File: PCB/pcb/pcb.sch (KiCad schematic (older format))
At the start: 13 parts, among them SW1 SW_Push, U1 ATmega32U4-AU, X1 Crystal_GND2

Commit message: Refactor controller layout.
Think that this is pretty much complete now.

Next up the matrix
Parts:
- removed R1: 10k, symbol Device:R
- removed X1: Crystal_GND2, symbol Device:Crystal_GND2
- added C7: 1u, symbol Device:C_Small
- added J1: USB_B_Micro, symbol Connector:USB_B_Micro
- added R1: 330, symbol Device:R_Small
- added R2: R_Small, symbol Device:R_Small
- added R3, R4: 10k, symbol Device:R_Small
- added Y1: 16MHz, symbol Device:Crystal_Small
- C1: renamed from C8; value 0.1u -> 11n
- R5: renamed from R2; value 10k -> 1k
- renumbered C3 to C2, C4 to C3, C1 to C4, C2 to C5, C5 to C6, C6 to C8, C7 to C9
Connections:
- net labels added: +5V, RST
- net labels removed: RESET, VCC, XTAL1, XTAL2
- wire segments 31 -> 47
- no-connect marks 0 -> 2
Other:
- note removed: "Crystal - Clock"
- note removed: "Reset button"
- note removed: "VCC - Decoupling caps"
- moved on the sheet: C1, C2, C3, C4, C5, C6, C8, C9, R5, SW1, U1

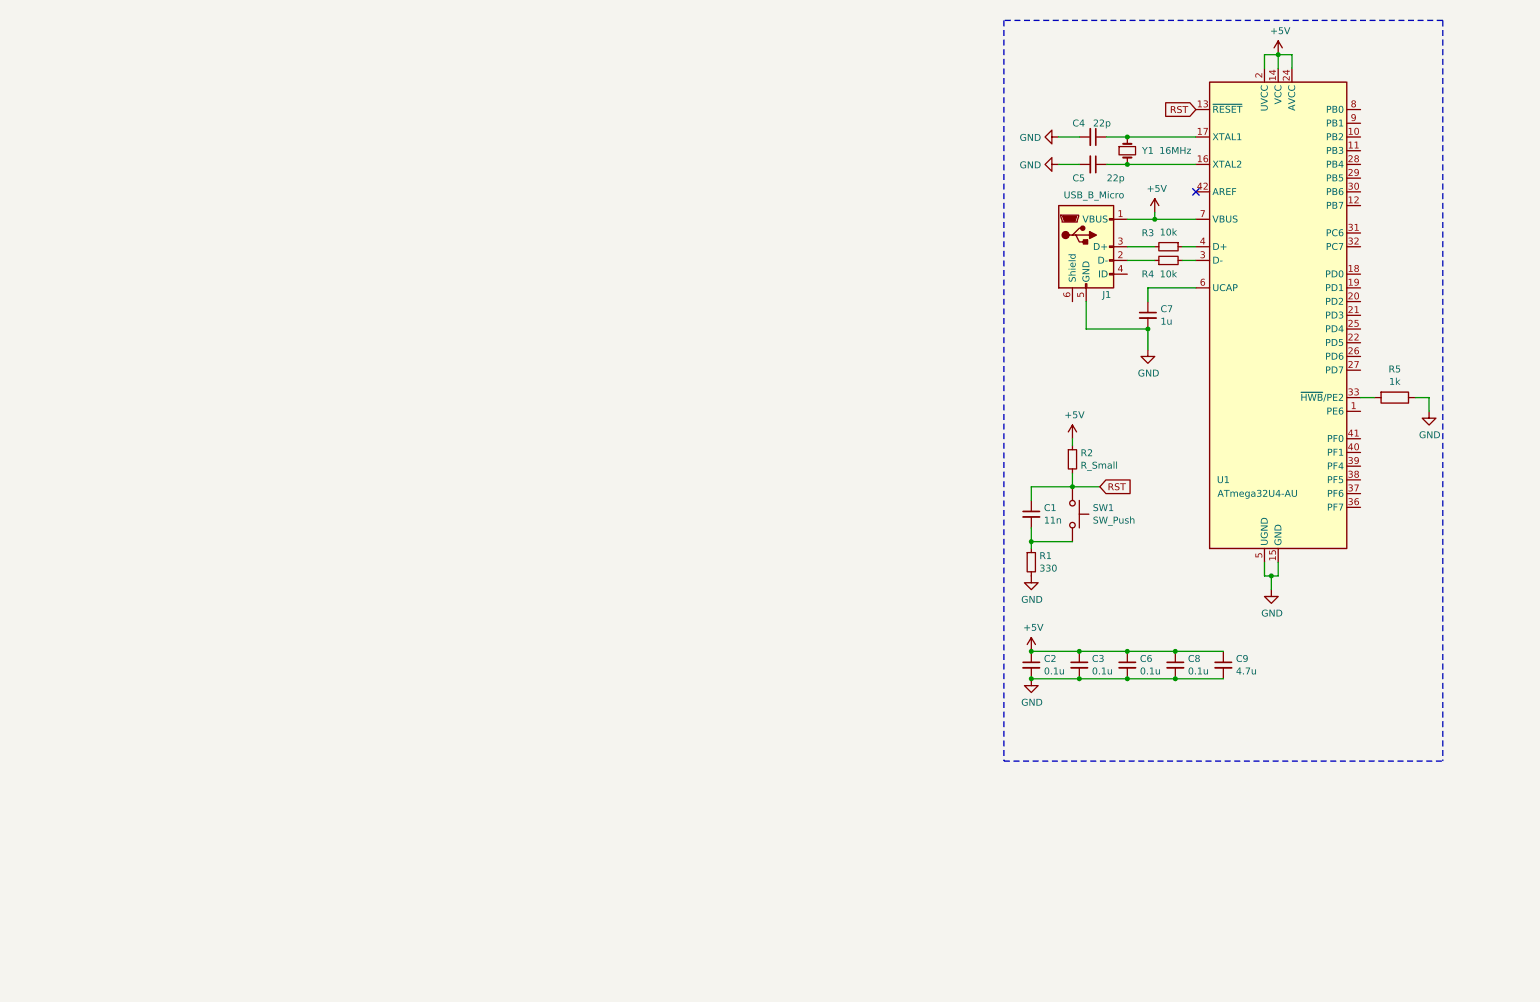
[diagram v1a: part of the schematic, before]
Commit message: Build the switch Matrix based on kbfirmwarebuilder
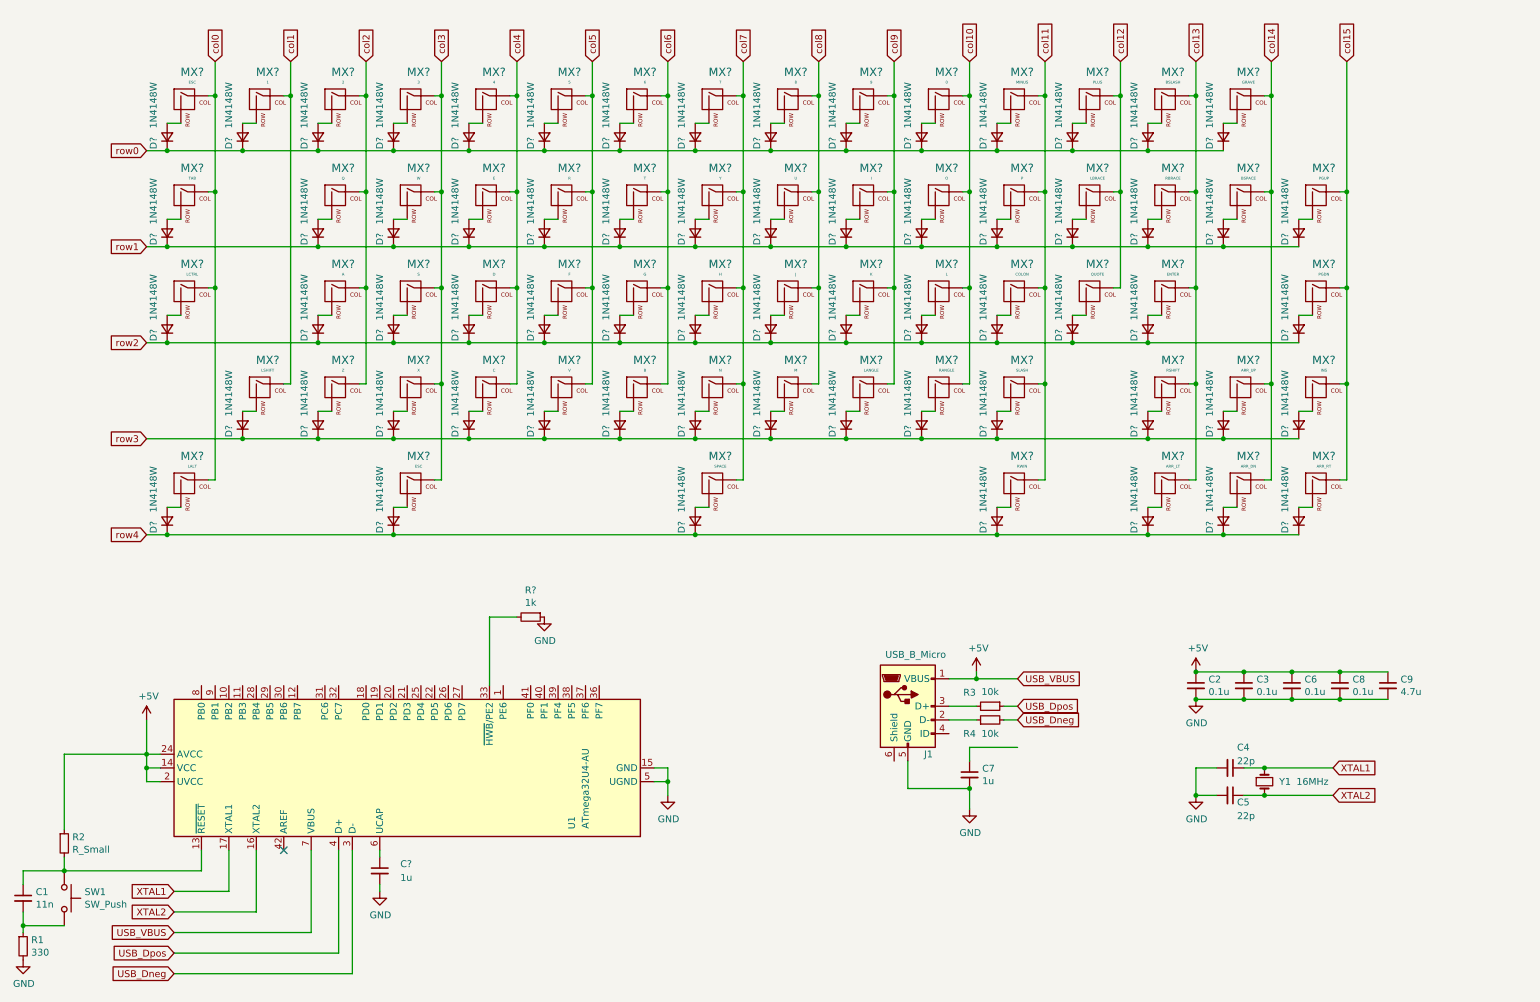
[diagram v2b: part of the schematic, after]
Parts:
- removed R5: 1k, symbol Device:R
- added C?: 1u, symbol Device:C_Small
- added D? (x65): 1N4148W, symbol Device:D_Small
- added MX? (x2): ESC, symbol MX_Alps_Hybrid:MX-NoLED
- added MX?: 1, symbol MX_Alps_Hybrid:MX-NoLED
- added MX?: 2, symbol MX_Alps_Hybrid:MX-NoLED
- added MX?: 3, symbol MX_Alps_Hybrid:MX-NoLED
- added MX?: 4, symbol MX_Alps_Hybrid:MX-NoLED
- added MX?: 5, symbol MX_Alps_Hybrid:MX-NoLED
- added MX?: 6, symbol MX_Alps_Hybrid:MX-NoLED
- added MX?: 7, symbol MX_Alps_Hybrid:MX-NoLED
- added MX?: 8, symbol MX_Alps_Hybrid:MX-NoLED
- added MX?: 9, symbol MX_Alps_Hybrid:MX-NoLED
- added MX?: 0, symbol MX_Alps_Hybrid:MX-NoLED
- added MX?: MINUS, symbol MX_Alps_Hybrid:MX-NoLED
- added MX?: PLUS, symbol MX_Alps_Hybrid:MX-NoLED
- added MX?: BSLASH, symbol MX_Alps_Hybrid:MX-NoLED
- added MX?: TAB, symbol MX_Alps_Hybrid:MX-NoLED
- added MX?: GRAVE, symbol MX_Alps_Hybrid:MX-NoLED
- added MX?: Q, symbol MX_Alps_Hybrid:MX-NoLED
- added MX?: W, symbol MX_Alps_Hybrid:MX-NoLED
- added MX?: E, symbol MX_Alps_Hybrid:MX-NoLED
- added MX?: R, symbol MX_Alps_Hybrid:MX-NoLED
- added MX?: T, symbol MX_Alps_Hybrid:MX-NoLED
- added MX?: Y, symbol MX_Alps_Hybrid:MX-NoLED
- added MX?: U, symbol MX_Alps_Hybrid:MX-NoLED
- added MX?: I, symbol MX_Alps_Hybrid:MX-NoLED
- added MX?: O, symbol MX_Alps_Hybrid:MX-NoLED
- added MX?: P, symbol MX_Alps_Hybrid:MX-NoLED
- added MX?: LBRACE, symbol MX_Alps_Hybrid:MX-NoLED
- added MX?: RBRACE, symbol MX_Alps_Hybrid:MX-NoLED
- added MX?: BSPACE, symbol MX_Alps_Hybrid:MX-NoLED
- added MX?: LCTRL, symbol MX_Alps_Hybrid:MX-NoLED
- added MX?: PGDN, symbol MX_Alps_Hybrid:MX-NoLED
- added MX?: A, symbol MX_Alps_Hybrid:MX-NoLED
- added MX?: S, symbol MX_Alps_Hybrid:MX-NoLED
- added MX?: D, symbol MX_Alps_Hybrid:MX-NoLED
- added MX?: F, symbol MX_Alps_Hybrid:MX-NoLED
- added MX?: G, symbol MX_Alps_Hybrid:MX-NoLED
- added MX?: H, symbol MX_Alps_Hybrid:MX-NoLED
- added MX?: J, symbol MX_Alps_Hybrid:MX-NoLED
- added MX?: K, symbol MX_Alps_Hybrid:MX-NoLED
- added MX?: L, symbol MX_Alps_Hybrid:MX-NoLED
- added MX?: COLON, symbol MX_Alps_Hybrid:MX-NoLED
- added MX?: QUOTE, symbol MX_Alps_Hybrid:MX-NoLED
- added MX?: ENTER, symbol MX_Alps_Hybrid:MX-NoLED
- added MX?: LSHIFT, symbol MX_Alps_Hybrid:MX-NoLED
- added MX?: INS, symbol MX_Alps_Hybrid:MX-NoLED
- added MX?: Z, symbol MX_Alps_Hybrid:MX-NoLED
- added MX?: X, symbol MX_Alps_Hybrid:MX-NoLED
- added MX?: C, symbol MX_Alps_Hybrid:MX-NoLED
- added MX?: V, symbol MX_Alps_Hybrid:MX-NoLED
- added MX?: B, symbol MX_Alps_Hybrid:MX-NoLED
- added MX?: N, symbol MX_Alps_Hybrid:MX-NoLED
- added MX?: M, symbol MX_Alps_Hybrid:MX-NoLED
- added MX?: LANGLE, symbol MX_Alps_Hybrid:MX-NoLED
- added MX?: RANGLE, symbol MX_Alps_Hybrid:MX-NoLED
- added MX?: SLASH, symbol MX_Alps_Hybrid:MX-NoLED
- added MX?: RSHIFT, symbol MX_Alps_Hybrid:MX-NoLED
- added MX?: ARR_UP, symbol MX_Alps_Hybrid:MX-NoLED
- added MX?: LALT, symbol MX_Alps_Hybrid:MX-NoLED
- added MX?: SPACE, symbol MX_Alps_Hybrid:MX-NoLED
- added MX?: RWIN, symbol MX_Alps_Hybrid:MX-NoLED
- added MX?: ARR_LT, symbol MX_Alps_Hybrid:MX-NoLED
- added MX?: ARR_DN, symbol MX_Alps_Hybrid:MX-NoLED
- added MX?: PGUP, symbol MX_Alps_Hybrid:MX-NoLED
- added MX?: ARR_RT, symbol MX_Alps_Hybrid:MX-NoLED
- added R?: 1k, symbol Device:R_Small
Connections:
- net GND: now also C?.2, R?.1
- net XTAL2: now reaches C5.1, U1.16 (XTAL2), Y1.2
- net XTAL1: now reaches C4.1, U1.17 (XTAL1), Y1.1
- net USB_Dneg: now reaches R4.2, U1.3 (D-)
- net at U1.33 (~HWB~/PE2): now also R?.2
- net USB_Dpos: now reaches R3.1, U1.4 (D+)
- net at U1.6 (UCAP): now also C?.1; no longer C7.1
- net RST: no longer names the net of C1.1, R2.2, SW1.1, U1.13 (~RESET)
- new net: D?.2 (A), MX?.2 (ROW) (x65)
- new net col0: MX?.1 (COL), MX?.1 (COL), MX?.1 (COL), MX?.1 (COL)
- new net col1: MX?.1 (COL), MX?.1 (COL)
- new net col10: MX?.1 (COL), MX?.1 (COL), MX?.1 (COL), MX?.1 (COL)
- new net col11: MX?.1 (COL), MX?.1 (COL), MX?.1 (COL), MX?.1 (COL), MX?.1 (COL)
- new net col12: MX?.1 (COL), MX?.1 (COL), MX?.1 (COL)
- new net col13: MX?.1 (COL), MX?.1 (COL), MX?.1 (COL), MX?.1 (COL), MX?.1 (COL)
- new net col14: MX?.1 (COL), MX?.1 (COL), MX?.1 (COL), MX?.1 (COL)
- new net col15: MX?.1 (COL), MX?.1 (COL), MX?.1 (COL), MX?.1 (COL)
- new net col2: MX?.1 (COL), MX?.1 (COL), MX?.1 (COL), MX?.1 (COL)
- new net col3: MX?.1 (COL), MX?.1 (COL), MX?.1 (COL), MX?.1 (COL), MX?.1 (COL)
- new net col4: MX?.1 (COL), MX?.1 (COL), MX?.1 (COL), MX?.1 (COL)
- new net col5: MX?.1 (COL), MX?.1 (COL), MX?.1 (COL), MX?.1 (COL)
- new net col6: MX?.1 (COL), MX?.1 (COL), MX?.1 (COL), MX?.1 (COL)
- new net col7: MX?.1 (COL), MX?.1 (COL), MX?.1 (COL), MX?.1 (COL), MX?.1 (COL)
- new net col8: MX?.1 (COL), MX?.1 (COL), MX?.1 (COL), MX?.1 (COL)
- new net col9: MX?.1 (COL), MX?.1 (COL), MX?.1 (COL), MX?.1 (COL)
- new net row0: D?.1 (K), D?.1 (K), D?.1 (K), D?.1 (K), D?.1 (K), D?.1 (K), D?.1 (K), D?.1 (K), D?.1 (K), D?.1 (K), D?.1 (K), D?.1 (K), D?.1 (K), D?.1 (K), D?.1 (K)
- new net row1: D?.1 (K), D?.1 (K), D?.1 (K), D?.1 (K), D?.1 (K), D?.1 (K), D?.1 (K), D?.1 (K), D?.1 (K), D?.1 (K), D?.1 (K), D?.1 (K), D?.1 (K), D?.1 (K), D?.1 (K)
- new net row2: D?.1 (K), D?.1 (K), D?.1 (K), D?.1 (K), D?.1 (K), D?.1 (K), D?.1 (K), D?.1 (K), D?.1 (K), D?.1 (K), D?.1 (K), D?.1 (K), D?.1 (K), D?.1 (K)
- new net row3: D?.1 (K), D?.1 (K), D?.1 (K), D?.1 (K), D?.1 (K), D?.1 (K), D?.1 (K), D?.1 (K), D?.1 (K), D?.1 (K), D?.1 (K), D?.1 (K), D?.1 (K), D?.1 (K)
- new net row4: D?.1 (K), D?.1 (K), D?.1 (K), D?.1 (K), D?.1 (K), D?.1 (K), D?.1 (K)
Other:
- moved on the sheet: C1, C2, C3, C4, C5, C6, C7, C8, C9, J1, R1, R2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

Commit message: reset annotations
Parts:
- removed C7: 1u, symbol Device:C_Small
- C1: value 11n -> 100n
- MX15: renamed from MX?; value ESC -> LWIN_1.5
- MX2: renamed from MX?; value TAB -> TAB_1.5
- MX3: renamed from MX?; value LCTRL -> LCTRL_1.75
- MX32: renamed from MX?; value SPACE -> SPACE_7flipped
- MX4: renamed from MX?; value LALT -> LALT_1.5
- MX49: renamed from MX?; value RWIN -> RWIN_1.5
- MX55: renamed from MX?; value ENTER -> ENTER_2.25
- MX56: renamed from MX?; value RSHIFT -> RSHIFT_1.75
- MX59: renamed from MX?; value BSPACE -> BSPACE_1.5
- MX6: renamed from MX?; value LSHIFT -> LSHIFT_2.25
- gave numbers to parts that had none: 122
- renumbered C9 to C10, C2 to C4, C4 to C5, C5 to C6, C3 to C7, C6 to C8, C8 to C9, R3 to R4, R4 to R5
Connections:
- net GND: now also C1.2, J1.6 (Shield)
- net col0: now also U1.29 (PB5)
- net col1: now also U1.30 (PB6)
- net col10: now also U1.22 (PD5)
- net col11: now also U1.26 (PD6)
- net col12: now also U1.27 (PD7)
- net col13: now also U1.41 (PF0)
- net col14: now also U1.40 (PF1)
- net col15: now also U1.39 (PF4)
- net col2: now also U1.12 (PB7)
- net col3: now also U1.31 (PC6)
- net col4: now also U1.32 (PC7)
- net col5: now also U1.18 (PD0)
- net col6: now also U1.19 (PD1)
- net col7: now also U1.20 (PD2)
- net col8: now also U1.21 (PD3)
- net col9: now also U1.25 (PD4)
- net row0: now also U1.8 (PB0)
- net row1: now also U1.9 (PB1)
- net row2: now also U1.10 (PB2)
- net row3: now also U1.11 (PB3)
- net row4: now also U1.28 (PB4)
- net at R1.1, SW1.2: no longer C1.2
- no-connect marks 2 -> 7
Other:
- moved on the sheet: R1

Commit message: Add footprints
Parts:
- C1, C10, C2, C4, C5, C6, C7, C8, C9: footprint (none) -> Capacitor_SMD:C_0805_2012Metric_Pad1.15x1.40mm_HandSolder
- D1, D10, D11, D12, D13, D14, D15, D16, D17, D18, D19, D2, D20, D21, D22, D23, D24, D25, D26, D27, D28, D29, D3, D30, D31, D32, D33, D34, D35, D36, D37, D38, D39, D4, D40, D41, D42, D43, D44, D45, D46, D47, D48, D49, D5, D50, D51, D52, D53, D54, D55, D56, D57, D58, D59, D6, D60, D61, D62, D63, D64, D65, D7, D8, D9: footprint (none) -> Diode_SMD:D_SOD-123
- J1: footprint (none) -> Connector_USB:USB_Micro-B_GCT_USB3076-30-A
- MX1, MX10, MX11, MX12, MX13, MX14, MX16, MX17, MX18, MX19, MX20, MX21, MX22, MX23, MX24, MX25, MX26, MX27, MX28, MX29, MX30, MX31, MX33, MX34, MX35, MX36, MX37, MX38, MX39, MX40, MX41, MX42, MX43, MX44, MX45, MX46, MX47, MX48, MX49, MX5, MX50, MX51, MX52, MX53, MX54, MX57, MX58, MX60, MX61, MX62, MX63, MX64, MX65, MX7, MX8, MX9: footprint (none) -> MX_Only:MXOnly-1U-NoLED
- MX15, MX2, MX4, MX59: footprint (none) -> MX_Only:MXOnly-1.5U-NoLED
- MX3, MX56: footprint (none) -> MX_Only:MXOnly-1.75U-NoLED
- MX32: footprint (none) -> MX_Only:MXOnly-7U-ReversedStabilizers
- MX55, MX6: footprint (none) -> MX_Only:MXOnly-2.25U-NoLED
- R1, R2, R3, R4, R5: footprint (none) -> Resistor_SMD:R_1206_3216Metric_Pad1.42x1.75mm_HandSolder
- SW1: footprint (none) -> Button_Switch_SMD:SW_SPST_B3S-1000
- Y1: footprint (none) -> Crystal:Crystal_SMD_5032-2Pin_5.0x3.2mm_HandSoldering

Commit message: PCB
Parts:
- MX49: footprint MX_Only:MXOnly-1U-NoLED -> MX_Only:MXOnly-1.5U-NoLED
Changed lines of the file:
@@
 F 0 "MX49" H 8033 4173 60  0000 C CNN
 F 1 "RWIN_1.5" H 8033 4099 20  0000 C CNN
-F 2 "MX_Only:MXOnly-1U-NoLED" H 7375 3925 60  0001 C CNN
+F 2 "MX_Only:MXOnly-1.5U-NoLED" H 7375 3925 60  0001 C CNN
 F 3 "" H 7375 3925 60  0001 C CNN
 	1    8000 3950

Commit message: Layout the switches and diodes
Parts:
- removed SW1: SW_Push, Button_Switch_SMD:SW_SPST_B3S-1000, symbol Switch:SW_Push
- removed Y1: 16MHz, Crystal:Crystal_SMD_5032-2Pin_5.0x3.2mm_HandSoldering, symbol Device:Crystal_Small
- added JP1: Jumper_NO_Small, Jumper:SolderJumper-2_P1.3mm_Open_RoundedPad1.0x1.5mm, symbol Device:Jumper_NO_Small
- added Y1: 16MHz, Crystal:Crystal_SMD_5032-4Pin_5.0x3.2mm, symbol Device:Crystal_GND24
- C1: renamed from C4; value 0.1u -> 1u
- C2: renamed from C7; value 0.1u -> 100n
- C3: renamed from C8; value 0.1u -> 100n
- C4: renamed from C9; value 0.1u -> 100n
- C5: renamed from C10; value 4.7u -> 100n
- MX1, MX39, MX56, MX65: symbol MX_Alps_Hybrid:MX-NoLED -> pcb-rescue:MX-NoLED-MX_Alps_Hybrid
- MX10: renamed from MX37; symbol MX_Alps_Hybrid:MX-NoLED -> pcb-rescue:MX-NoLED-MX_Alps_Hybrid
- MX11: renamed from MX41; symbol MX_Alps_Hybrid:MX-NoLED -> pcb-rescue:MX-NoLED-MX_Alps_Hybrid
- MX12: renamed from MX45; symbol MX_Alps_Hybrid:MX-NoLED -> pcb-rescue:MX-NoLED-MX_Alps_Hybrid
- MX13: renamed from MX50; symbol MX_Alps_Hybrid:MX-NoLED -> pcb-rescue:MX-NoLED-MX_Alps_Hybrid
- MX14: renamed from MX53; symbol MX_Alps_Hybrid:MX-NoLED -> pcb-rescue:MX-NoLED-MX_Alps_Hybrid
- MX15: renamed from MX58; symbol MX_Alps_Hybrid:MX-NoLED -> pcb-rescue:MX-NoLED-MX_Alps_Hybrid
- MX16: renamed from MX2; symbol MX_Alps_Hybrid:MX-NoLED -> pcb-rescue:MX-NoLED-MX_Alps_Hybrid
- MX17: renamed from MX8; symbol MX_Alps_Hybrid:MX-NoLED -> pcb-rescue:MX-NoLED-MX_Alps_Hybrid
- MX18: renamed from MX12; symbol MX_Alps_Hybrid:MX-NoLED -> pcb-rescue:MX-NoLED-MX_Alps_Hybrid
- MX19: renamed from MX17; symbol MX_Alps_Hybrid:MX-NoLED -> pcb-rescue:MX-NoLED-MX_Alps_Hybrid
- MX2: renamed from MX5; symbol MX_Alps_Hybrid:MX-NoLED -> pcb-rescue:MX-NoLED-MX_Alps_Hybrid
- MX20: renamed from MX21; symbol MX_Alps_Hybrid:MX-NoLED -> pcb-rescue:MX-NoLED-MX_Alps_Hybrid
- MX21: renamed from MX25; symbol MX_Alps_Hybrid:MX-NoLED -> pcb-rescue:MX-NoLED-MX_Alps_Hybrid
- MX22: renamed from MX29; symbol MX_Alps_Hybrid:MX-NoLED -> pcb-rescue:MX-NoLED-MX_Alps_Hybrid
- MX23: renamed from MX34; symbol MX_Alps_Hybrid:MX-NoLED -> pcb-rescue:MX-NoLED-MX_Alps_Hybrid
- MX24: renamed from MX38; symbol MX_Alps_Hybrid:MX-NoLED -> pcb-rescue:MX-NoLED-MX_Alps_Hybrid
- MX25: renamed from MX42; symbol MX_Alps_Hybrid:MX-NoLED -> pcb-rescue:MX-NoLED-MX_Alps_Hybrid
- MX26: renamed from MX46; symbol MX_Alps_Hybrid:MX-NoLED -> pcb-rescue:MX-NoLED-MX_Alps_Hybrid
- MX27: renamed from MX51; symbol MX_Alps_Hybrid:MX-NoLED -> pcb-rescue:MX-NoLED-MX_Alps_Hybrid
- MX28: renamed from MX54; symbol MX_Alps_Hybrid:MX-NoLED -> pcb-rescue:MX-NoLED-MX_Alps_Hybrid
- MX29: renamed from MX59; symbol MX_Alps_Hybrid:MX-NoLED -> pcb-rescue:MX-NoLED-MX_Alps_Hybrid
- MX3: renamed from MX7; symbol MX_Alps_Hybrid:MX-NoLED -> pcb-rescue:MX-NoLED-MX_Alps_Hybrid
- MX30: renamed from MX62; symbol MX_Alps_Hybrid:MX-NoLED -> pcb-rescue:MX-NoLED-MX_Alps_Hybrid
- MX31: renamed from MX3; symbol MX_Alps_Hybrid:MX-NoLED -> pcb-rescue:MX-NoLED-MX_Alps_Hybrid
- MX32: renamed from MX9; symbol MX_Alps_Hybrid:MX-NoLED -> pcb-rescue:MX-NoLED-MX_Alps_Hybrid
- MX33: renamed from MX13; symbol MX_Alps_Hybrid:MX-NoLED -> pcb-rescue:MX-NoLED-MX_Alps_Hybrid
- MX34: renamed from MX18; symbol MX_Alps_Hybrid:MX-NoLED -> pcb-rescue:MX-NoLED-MX_Alps_Hybrid
- MX35: renamed from MX22; symbol MX_Alps_Hybrid:MX-NoLED -> pcb-rescue:MX-NoLED-MX_Alps_Hybrid
- MX36: renamed from MX26; symbol MX_Alps_Hybrid:MX-NoLED -> pcb-rescue:MX-NoLED-MX_Alps_Hybrid
- MX37: renamed from MX30; symbol MX_Alps_Hybrid:MX-NoLED -> pcb-rescue:MX-NoLED-MX_Alps_Hybrid
- MX38: renamed from MX35; symbol MX_Alps_Hybrid:MX-NoLED -> pcb-rescue:MX-NoLED-MX_Alps_Hybrid
- MX4: renamed from MX11; symbol MX_Alps_Hybrid:MX-NoLED -> pcb-rescue:MX-NoLED-MX_Alps_Hybrid
- MX40: renamed from MX43; symbol MX_Alps_Hybrid:MX-NoLED -> pcb-rescue:MX-NoLED-MX_Alps_Hybrid
- MX41: renamed from MX47; symbol MX_Alps_Hybrid:MX-NoLED -> pcb-rescue:MX-NoLED-MX_Alps_Hybrid
- MX42: renamed from MX52; symbol MX_Alps_Hybrid:MX-NoLED -> pcb-rescue:MX-NoLED-MX_Alps_Hybrid
- MX43: renamed from MX55; symbol MX_Alps_Hybrid:MX-NoLED -> pcb-rescue:MX-NoLED-MX_Alps_Hybrid
- MX44: renamed from MX63; symbol MX_Alps_Hybrid:MX-NoLED -> pcb-rescue:MX-NoLED-MX_Alps_Hybrid
- MX45: renamed from MX6; symbol MX_Alps_Hybrid:MX-NoLED -> pcb-rescue:MX-NoLED-MX_Alps_Hybrid
- MX46: renamed from MX10; symbol MX_Alps_Hybrid:MX-NoLED -> pcb-rescue:MX-NoLED-MX_Alps_Hybrid
- MX47: renamed from MX14; symbol MX_Alps_Hybrid:MX-NoLED -> pcb-rescue:MX-NoLED-MX_Alps_Hybrid
- MX48: renamed from MX19; symbol MX_Alps_Hybrid:MX-NoLED -> pcb-rescue:MX-NoLED-MX_Alps_Hybrid
- MX49: renamed from MX23; symbol MX_Alps_Hybrid:MX-NoLED -> pcb-rescue:MX-NoLED-MX_Alps_Hybrid
- MX5: renamed from MX16; symbol MX_Alps_Hybrid:MX-NoLED -> pcb-rescue:MX-NoLED-MX_Alps_Hybrid
- MX50: renamed from MX27; symbol MX_Alps_Hybrid:MX-NoLED -> pcb-rescue:MX-NoLED-MX_Alps_Hybrid
- MX51: renamed from MX31; symbol MX_Alps_Hybrid:MX-NoLED -> pcb-rescue:MX-NoLED-MX_Alps_Hybrid
- MX52: renamed from MX36; symbol MX_Alps_Hybrid:MX-NoLED -> pcb-rescue:MX-NoLED-MX_Alps_Hybrid
- MX53: renamed from MX40; symbol MX_Alps_Hybrid:MX-NoLED -> pcb-rescue:MX-NoLED-MX_Alps_Hybrid
- MX54: renamed from MX44; symbol MX_Alps_Hybrid:MX-NoLED -> pcb-rescue:MX-NoLED-MX_Alps_Hybrid
- MX55: renamed from MX48; symbol MX_Alps_Hybrid:MX-NoLED -> pcb-rescue:MX-NoLED-MX_Alps_Hybrid
- MX57: renamed from MX60; symbol MX_Alps_Hybrid:MX-NoLED -> pcb-rescue:MX-NoLED-MX_Alps_Hybrid
- MX58: renamed from MX64; symbol MX_Alps_Hybrid:MX-NoLED -> pcb-rescue:MX-NoLED-MX_Alps_Hybrid
- MX59: renamed from MX4; symbol MX_Alps_Hybrid:MX-NoLED -> pcb-rescue:MX-NoLED-MX_Alps_Hybrid
- MX6: renamed from MX20; symbol MX_Alps_Hybrid:MX-NoLED -> pcb-rescue:MX-NoLED-MX_Alps_Hybrid
- MX60: renamed from MX15; symbol MX_Alps_Hybrid:MX-NoLED -> pcb-rescue:MX-NoLED-MX_Alps_Hybrid
- MX61: renamed from MX32; footprint MX_Only:MXOnly-7U-ReversedStabilizers -> MX_Only:MXOnly-7U-ReversedStabilizers-NoLED; symbol MX_Alps_Hybrid:MX-NoLED -> pcb-rescue:MX-NoLED-MX_Alps_Hybrid
- MX62: renamed from MX49; symbol MX_Alps_Hybrid:MX-NoLED -> pcb-rescue:MX-NoLED-MX_Alps_Hybrid
- MX63: renamed from MX57; symbol MX_Alps_Hybrid:MX-NoLED -> pcb-rescue:MX-NoLED-MX_Alps_Hybrid
- MX64: renamed from MX61; symbol MX_Alps_Hybrid:MX-NoLED -> pcb-rescue:MX-NoLED-MX_Alps_Hybrid
- MX7: renamed from MX24; symbol MX_Alps_Hybrid:MX-NoLED -> pcb-rescue:MX-NoLED-MX_Alps_Hybrid
- MX8: renamed from MX28; symbol MX_Alps_Hybrid:MX-NoLED -> pcb-rescue:MX-NoLED-MX_Alps_Hybrid
- MX9: renamed from MX33; symbol MX_Alps_Hybrid:MX-NoLED -> pcb-rescue:MX-NoLED-MX_Alps_Hybrid
- renumbered C5 to C6, C6 to C7, C2 to C8, C1 to C9, D37 to D10, D41 to D11, D45 to D12, D50 to D13, D53 to D14, D58 to D15, D2 to D16, D8 to D17, D12 to D18, D17 to D19, D5 to D2, D21 to D20, D25 to D21, D29 to D22, D34 to D23, D38 to D24, D42 to D25, D46 to D26, D51 to D27, D54 to D28, D59 to D29, D7 to D3, D62 to D30, D3 to D31, D9 to D32, D13 to D33, D18 to D34, D22 to D35, D26 to D36, D30 to D37, D35 to D38, D11 to D4, D43 to D40, D47 to D41, D52 to D42, D55 to D43, D63 to D44, D6 to D45, D10 to D46, D14 to D47, D19 to D48, D23 to D49, D16 to D5, D27 to D50, D31 to D51, D36 to D52, D40 to D53, D44 to D54, D48 to D55, D60 to D57, D64 to D58, D4 to D59, D20 to D6, D15 to D60, D32 to D61, D49 to D62, D57 to D63, D61 to D64, D24 to D7, D28 to D8, D33 to D9, R3 to R1, R4 to R2, R5 to R3, R2 to R4, R1 to R5
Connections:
- net GND: now also Y1.2, Y1.4
- net XTAL1: now also Y1.1
- net XTAL2: now also Y1.3
- net col0: now also U1.8 (PB0); no longer U1.29 (PB5)
- net col1: now also U1.9 (PB1); no longer U1.30 (PB6)
- net col10: now also U1.32 (PC7); no longer U1.22 (PD5)
- net col11: now also U1.31 (PC6); no longer U1.26 (PD6)
- net col12: now also U1.30 (PB6); no longer U1.27 (PD7)
- net col13: now also U1.29 (PB5); no longer U1.41 (PF0)
- net col14: now also U1.28 (PB4); no longer U1.40 (PF1)
- net col15: now also U1.27 (PD7); no longer U1.39 (PF4)
- net col2: now also U1.10 (PB2); no longer U1.12 (PB7)
- net col3: now also U1.11 (PB3); no longer U1.31 (PC6)
- net col4: now also U1.41 (PF0); no longer U1.32 (PC7)
- net col5: now also U1.40 (PF1); no longer U1.18 (PD0)
- net col6: now also U1.39 (PF4); no longer U1.19 (PD1)
- net col7: now also U1.38 (PF5); no longer U1.20 (PD2)
- net col8: now also U1.37 (PF6); no longer U1.21 (PD3)
- net col9: now also U1.36 (PF7); no longer U1.25 (PD4)
- net row0: now also U1.19 (PD1); no longer U1.8 (PB0)
- net row1: now also U1.20 (PD2); no longer U1.9 (PB1)
- net row2: now also U1.21 (PD3); no longer U1.10 (PB2)
- net row3: now also U1.22 (PD5); no longer U1.11 (PB3)
- net row4: now also U1.18 (PD0); no longer U1.28 (PB4)
- net at C9.1, R4.2, U1.13 (~RESET): now also JP1.1
- net at R5.1: now also JP1.2
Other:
- moved on the sheet: C7
